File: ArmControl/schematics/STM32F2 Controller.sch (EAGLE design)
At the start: 97 parts, among them IC1 REG1117, IC2 TL072D, IC3 TL072D, Q301 BC846, Q701 BC846, U1 STM32F10XRXT6

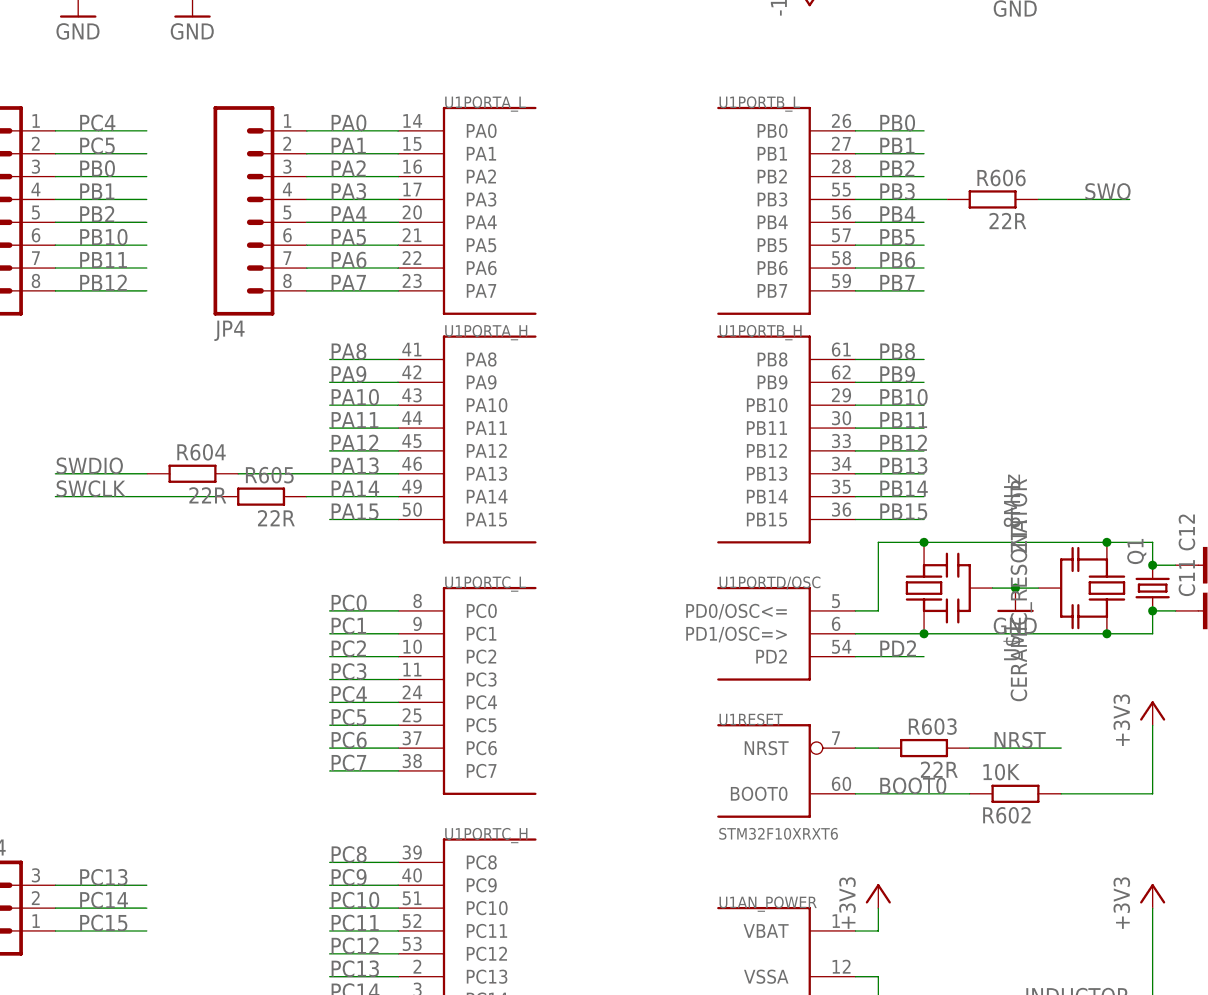
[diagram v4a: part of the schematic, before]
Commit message: added and layed out labels
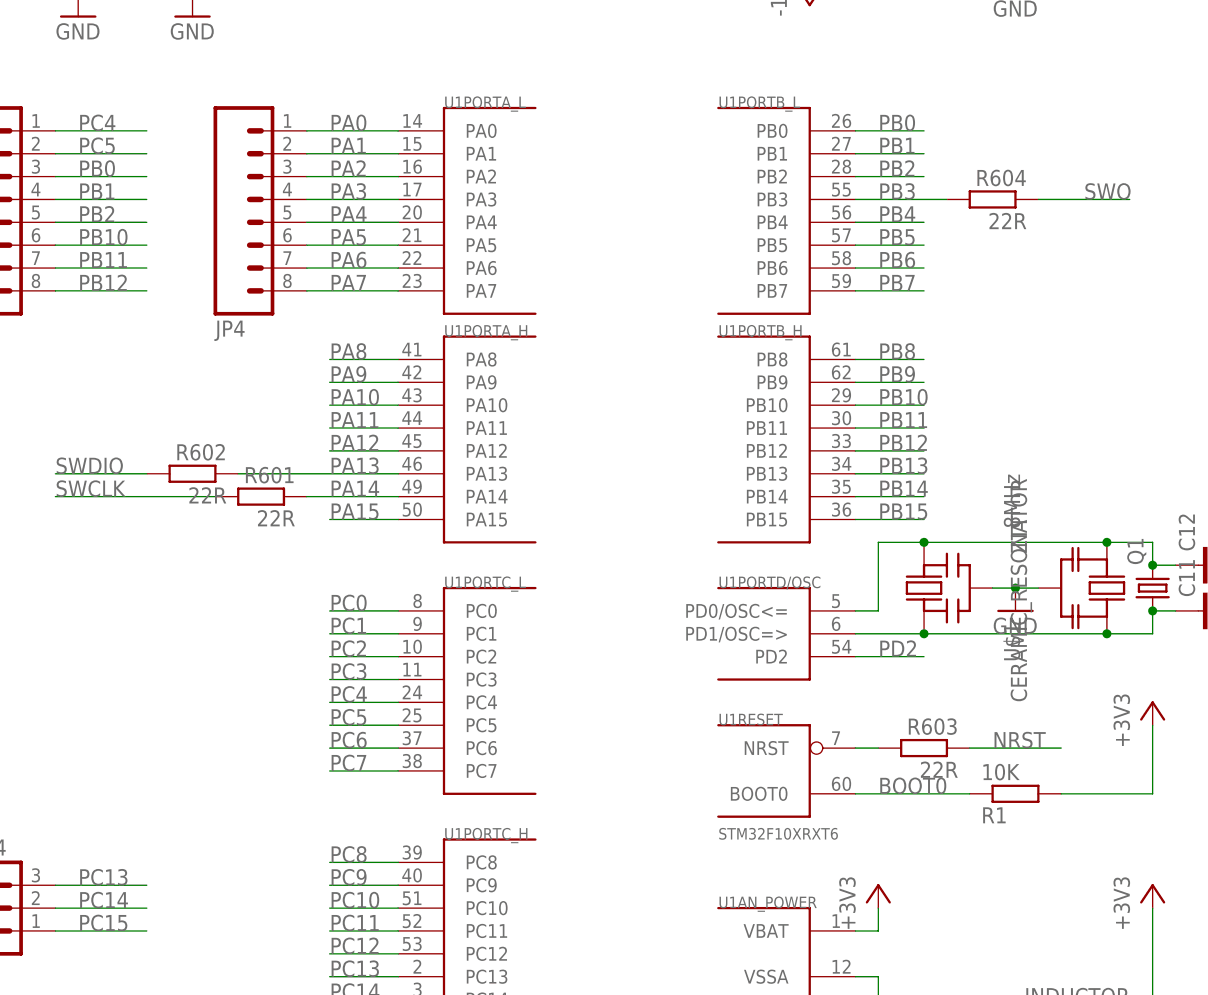
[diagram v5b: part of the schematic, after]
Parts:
- removed R606: 22R, resistor:R-EU_R0603
- added R1: 10K, resistor:R-EU_R0603
- R602: value 10K -> 22R
- renumbered R605 to R601
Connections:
- net +3V3: now also R1.2; no longer R602.2
- net BOOT0: now also R1.1; no longer R602.1
- net PA13: now also R602.1; no longer R604.1
- net PB3: now also R604.2; no longer R606.2
- net SWDIO: now also R602.2; no longer R604.2
- net SWO: now also R604.1; no longer R606.1
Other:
- moved on the sheet: R602, R604
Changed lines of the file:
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@@
 <part name="+3V2" library="supply1" deviceset="+3V3" device=""/>
 <part name="GND5" library="supply1" deviceset="GND" device=""/>
-<part name="R602" library="resistor" deviceset="R-EU_" device="R0603" value="10K"/>
+<part name="R1" library="resistor" deviceset="R-EU_" device="R0603" value="10K"/>
 <part name="GND7" library="supply1" deviceset="GND" device=""/>
 <part name="L1" library="Rebel" deviceset="INDUCTOR" device=""/>
@@
 <part name="+3V5" library="supply1" deviceset="+3V3" device=""/>
 <part name="R603" library="resistor" deviceset="R-EU_" device="R0603" value="22R"/>
+<part name="R602" library="resistor" deviceset="R-EU_" device="R0603" value="22R"/>
+<part name="R601" library="resistor" deviceset="R-EU_" device="R0603" value="22R"/>
 <part name="R604" library="resistor" deviceset="R-EU_" device="R0603" value="22R"/>
-<part name="R605" library="resistor" deviceset="R-EU_" device="R0603" value="22R"/>
-<part name="R606" library="resistor" deviceset="R-EU_" device="R0603" value="22R"/>
 <part name="GND9" library="supply1" deviceset="GND" device=""/>
 <part name="GND10" library="supply1" deviceset="GND" device=""/>
@@
 <instance part="+3V2" gate="G$1" x="187.96" y="20.32"/>
 <instance part="GND5" gate="1" x="187.96" y="-30.48"/>
-<instance part="R602" gate="G$1" x="106.68" y="-5.08" rot="MR180"/>
+<instance part="R1" gate="G$1" x="106.68" y="-5.08" rot="MR180"/>
 <instance part="GND7" gate="1" x="91.44" y="-50.8"/>
 <instance part="L1" gate="G$1" x="114.3" y="-30.48"/>
@@
 <instance part="+3V5" gate="G$1" x="269.24" y="66.04"/>
 <instance part="R603" gate="G$1" x="96.52" y="0" rot="MR0"/>
-<instance part="R604" gate="G$1" x="15.24" y="30.48" rot="MR0"/>
-<instance part="R605" gate="G$1" x="22.86" y="27.94" rot="MR0"/>
-<instance part="R606" gate="G$1" x="104.14" y="60.96" rot="MR0"/>
+<instance part="R602" gate="G$1" x="15.24" y="30.48" rot="MR0"/>
+<instance part="R601" gate="G$1" x="22.86" y="27.94" rot="MR0"/>
+<instance part="R604" gate="G$1" x="104.14" y="60.96" rot="MR0"/>
 <instance part="GND9" gate="1" x="172.72" y="-30.48"/>
 <instance part="GND10" gate="1" x="162.56" y="-30.48"/>
@@
 </segment>
 <segment>
-<pinref part="R604" gate="G$1" pin="2"/>
+<pinref part="R602" gate="G$1" pin="2"/>
 <wire x1="10.16" y1="30.48" x2="0" y2="30.48" width="0.1524" layer="91"/>
 <label x="0" y="30.48" size="1.778" layer="95"/>
@@
 </segment>
 <segment>
-<pinref part="R606" gate="G$1" pin="1"/>
+<pinref part="R604" gate="G$1" pin="1"/>
 <wire x1="109.22" y1="60.96" x2="119.38" y2="60.96" width="0.1524" layer="91"/>
 <label x="114.3" y="60.96" size="1.778" layer="95"/>
@@
 </segment>
 <segment>
-<pinref part="R602" gate="G$1" pin="2"/>
+<pinref part="R1" gate="G$1" pin="2"/>
 <pinref part="+3V1" gate="G$1" pin="+3V3"/>
 <wire x1="111.76" y1="-5.08" x2="121.92" y2="-5.08" width="0.1524" layer="91"/>
@@
 </segment>
 <segment>
-<pinref part="R605" gate="G$1" pin="2"/>
+<pinref part="R601" gate="G$1" pin="2"/>
 <wire x1="17.78" y1="27.94" x2="0" y2="27.94" width="0.1524" layer="91"/>
 <label x="0" y="27.94" size="1.778" layer="95"/>
@@
 <segment>
 <pinref part="U1" gate="PORTA_H" pin="PA13"/>
-<pinref part="R604" gate="G$1" pin="1"/>
+<pinref part="R602" gate="G$1" pin="1"/>
 <wire x1="20.32" y1="30.48" x2="38.1" y2="30.48" width="0.1524" layer="91"/>
 <label x="30.48" y="30.48" size="1.778" layer="95"/>
@@
 <segment>
 <pinref part="U1" gate="PORTA_H" pin="PA14"/>
-<pinref part="R605" gate="G$1" pin="1"/>
+<pinref part="R601" gate="G$1" pin="1"/>
 <wire x1="27.94" y1="27.94" x2="38.1" y2="27.94" width="0.1524" layer="91"/>
 <label x="30.48" y="27.94" size="1.778" layer="95"/>
@@
 <segment>
 <pinref part="U1" gate="PORTB_L" pin="PB3"/>
-<pinref part="R606" gate="G$1" pin="2"/>
+<pinref part="R604" gate="G$1" pin="2"/>
 <wire x1="99.06" y1="60.96" x2="88.9" y2="60.96" width="0.1524" layer="91"/>
 <label x="91.44" y="60.96" size="1.778" layer="95"/>
@@
 <segment>
 <pinref part="U1" gate="RESET" pin="BOOT0"/>
-<pinref part="R602" gate="G$1" pin="1"/>
+<pinref part="R1" gate="G$1" pin="1"/>
 <wire x1="88.9" y1="-5.08" x2="101.6" y2="-5.08" width="0.1524" layer="91"/>
 <label x="91.44" y="-5.08" size="1.778" layer="95"/>

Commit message: tons of old updates in one fat commit
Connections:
- net N$12 renamed RST
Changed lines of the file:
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@@
 </segment>
 </net>
-<net name="N$12" class="0">
+<net name="RST" class="0">
 <segment>
 <pinref part="U1" gate="RESET" pin="NRST"/>
